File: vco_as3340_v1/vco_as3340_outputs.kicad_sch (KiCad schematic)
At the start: 28 parts, among them J102 SAWTOOTH, J103 TRIANGLE, J104 PULSE, U4 TL072, U5 TL072

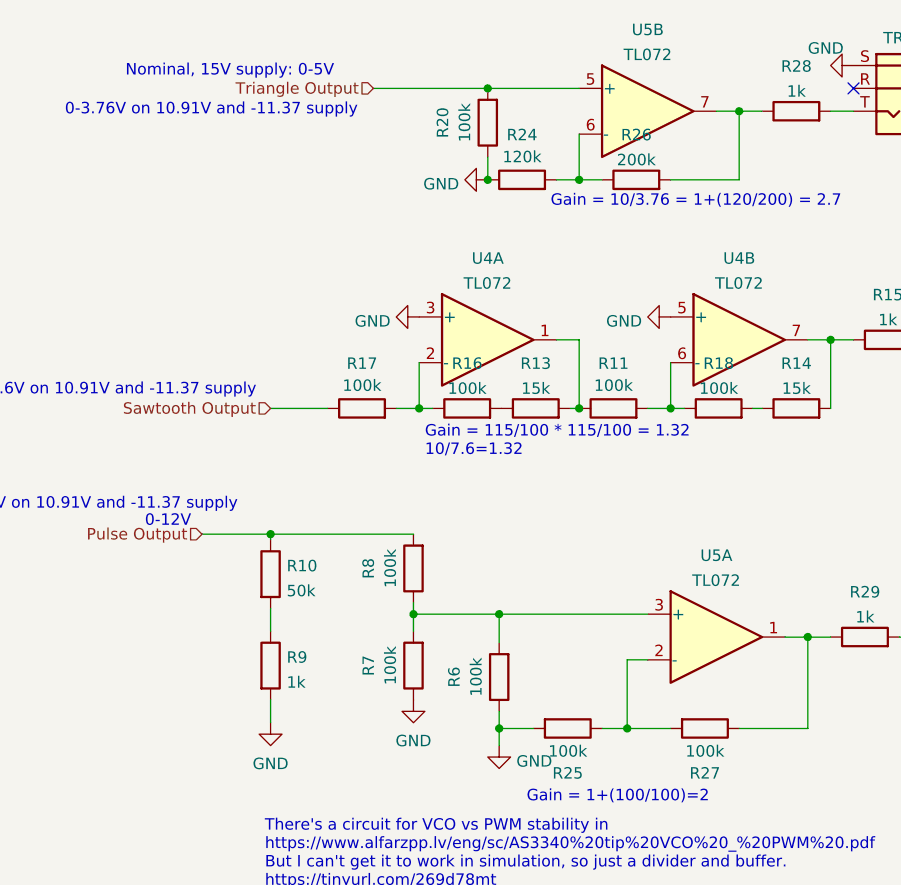
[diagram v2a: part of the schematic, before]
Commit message: Schematic Changes v1 to v2
 - R10 = 47k
 - R9 = 0ohm
 - New C1 100pF across R10 and R9
 - New C15 10uF polarized cap from -5 to GND.
 - R6 DNU
 - R21 & R23 changed to 5.1k
 - RZ1 changed to 18k
 - R26 changed to 100k and new R31 is 100k.
 - New  R32 for 'hysteresis' between PWM and Pulse.
 - Separated grounds on Linear FM and Scale Adj. Circuits for clarity.
 - Added another TL072 (U6) and supporting circuits.
    - This is intended to supply two reference voltages from the 5V
source.
    - The idea is to provide Soft Sync (pin 9) with a stable voltage
of 1/3*Supply, which is something like 11.3/3.
    - The other REF_PITCH2 is for the Linear FM circuit. Some resistors
probably aren't right for this yet, and I think it can completely
replace REF_PITCH pot so I've placed a jumper there to allow either if
it doesn't work out.
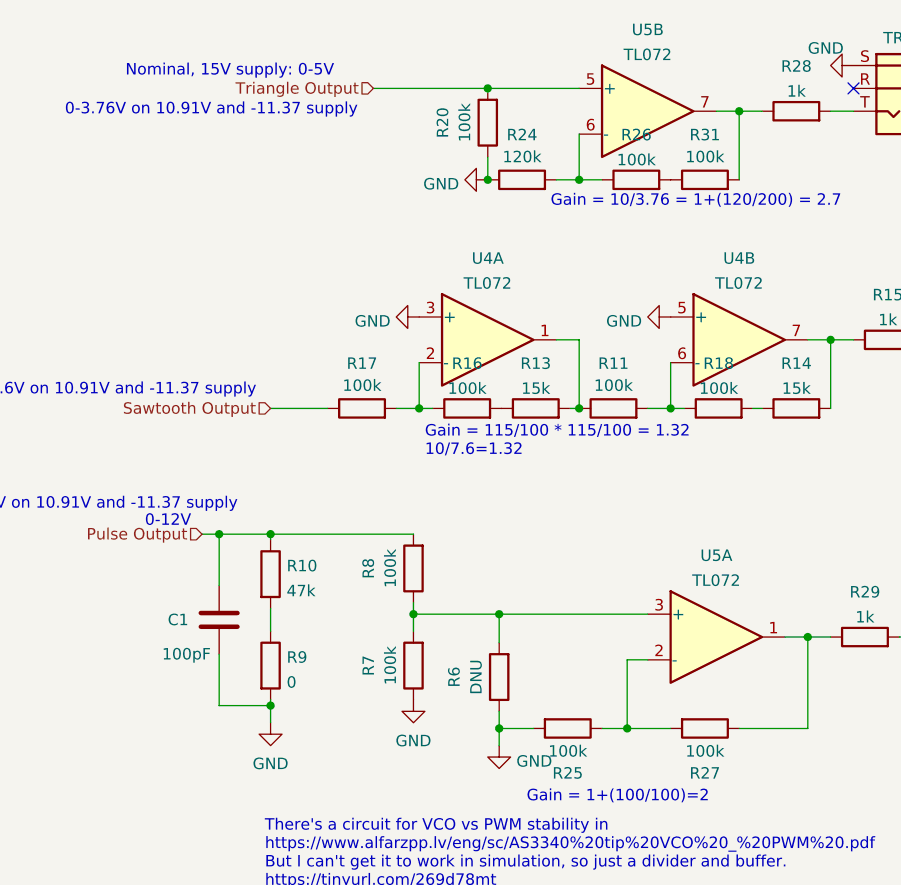
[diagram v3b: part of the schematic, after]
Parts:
- added C1: 100pF, Capacitor_SMD:C_1206_3216Metric_Pad1.33x1.80mm_HandSolder, symbol Device:C
- added R31: 100k, Resistor_SMD:R_1206_3216Metric_Pad1.30x1.75mm_HandSolder, symbol Device:R
- R10: value 50k -> 47k
- R26: value 200k -> 100k
- R6: value 100k -> DNU
- R9: value 1k -> 0
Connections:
- net GND: now also C1.2
- net Pulse Output: now also C1.1
- net at R28.1, U5.7: now also R31.2; no longer R26.2
- new net: R26.2, R31.1
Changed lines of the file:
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@@
     (company "RobotDialogs")
   )
+  (junction (at 77.47 91.44) (diameter 0) (color 0 0 0 0)
+  )
   (junction (at 129.54 25.4) (diameter 0) (color 0 0 0 0)
   )
@@
   )
   (junction (at 111.76 33.02) (diameter 0) (color 0 0 0 0)
+  )
+  (junction (at 71.755 72.39) (diameter 0) (color 0 0 0 0)
   )
   (junction (at 133.985 158.75) (diameter 0) (color 0 0 0 0)
@@
     (stroke (width 0) (type default) (color 0 0 0 0))
   )
+  (wire (pts (xy 71.755 91.44) (xy 77.47 91.44))
+    (stroke (width 0) (type default) (color 0 0 0 0))
+  )
   (wire (pts (xy 109.22 33.02) (xy 111.76 33.02))
     (stroke (width 0) (type default) (color 0 0 0 0))
@@
     (stroke (width 0) (type default) (color 0 0 0 0))
   )
+  (wire (pts (xy 71.755 85.725) (xy 71.755 91.44))
+    (stroke (width 0) (type default) (color 0 0 0 0))
+  )
   (wire (pts (xy 119.38 58.42) (xy 121.92 58.42))
     (stroke (width 0) (type default) (color 0 0 0 0))
@@
     (stroke (width 0) (type default) (color 0 0 0 0))
   )
-  (wire (pts (xy 69.85 72.39) (xy 77.47 72.39))
+  (wire (pts (xy 69.85 72.39) (xy 71.755 72.39))
     (stroke (width 0) (type default) (color 0 0 0 0))
   )
@@
     (stroke (width 0) (type default) (color 0 0 0 0))
   )
-  (wire (pts (xy 121.92 33.02) (xy 129.54 33.02))
-    (stroke (width 0) (type default) (color 0 0 0 0))
-  )
   (wire (pts (xy 93.98 53.34) (xy 93.98 58.42))
     (stroke (width 0) (type default) (color 0 0 0 0))
@@
     (stroke (width 0) (type default) (color 0 0 0 0))
   )
+  (wire (pts (xy 77.47 91.44) (xy 77.47 90.805))
+    (stroke (width 0) (type default) (color 0 0 0 0))
+  )
   (wire (pts (xy 153.67 83.82) (xy 147.32 83.82))
     (stroke (width 0) (type default) (color 0 0 0 0))
@@
     (stroke (width 0) (type default) (color 0 0 0 0))
   )
+  (wire (pts (xy 71.755 78.105) (xy 71.755 72.39))
+    (stroke (width 0) (type default) (color 0 0 0 0))
+  )
   (wire (pts (xy 91.44 58.42) (xy 93.98 58.42))
     (stroke (width 0) (type default) (color 0 0 0 0))
@@
     (stroke (width 0) (type default) (color 0 0 0 0))
   )
+  (wire (pts (xy 71.755 72.39) (xy 77.47 72.39))
+    (stroke (width 0) (type default) (color 0 0 0 0))
+  )
   (wire (pts (xy 102.87 84.455) (xy 102.87 81.28))
     (stroke (width 0) (type default) (color 0 0 0 0))
@@
     (stroke (width 0) (type default) (color 0 0 0 0))
   )
-  (wire (pts (xy 77.47 93.345) (xy 77.47 90.805))
+  (wire (pts (xy 77.47 93.345) (xy 77.47 91.44))
     (stroke (width 0) (type default) (color 0 0 0 0))
   )
@@
     (in_bom yes) (on_board yes) (fields_autoplaced)
     (property "Reference" "R26" (id 0) (at 118.11 28.0375 90))
-    (property "Value" "200k" (id 1) (at 118.11 30.8126 90))
+    (property "Value" "100k" (id 1) (at 118.11 30.8126 90))
     (property "Footprint" "Resistor_SMD:R_1206_3216Metric_Pad1.30x1.75mm_HandSolder" (id 2) (at 118.11 34.798 90)
       (effects (font (size 1.27 1.27)) hide)
@@
     (pin "2")
   )
+  (symbol (lib_id "Device:C") (at 71.755 81.915 0) (unit 1)
+    (in_bom yes) (on_board yes)
+    (property "Reference" "C1" (id 0) (at 66.04 81.915 0)
+      (effects (font (size 1.27 1.27)) (justify left))
+    )
+    (property "Value" "100pF" (id 1) (at 65.405 85.725 0)
+      (effects (font (size 1.27 1.27)) (justify left))
+    )
+    (property "Footprint" "Capacitor_SMD:C_1206_3216Metric_Pad1.33x1.80mm_HandSolder" (id 2) (at 72.7202 85.725 0)
+      (effects (font (size 1.27 1.27)) hide)
+    )
+    (property "Datasheet" "~" (id 3) (at 71.755 81.915 0)
+      (effects (font (size 1.27 1.27)) hide)
+    )
+    (pin "1")
+    (pin "2")
+  )
   (symbol (lib_id "Device:R") (at 77.47 86.995 0) (unit 1)
     (in_bom yes) (on_board yes) (fields_autoplaced)
@@
       (effects (font (size 1.27 1.27)) (justify left))
     )
-    (property "Value" "1k" (id 1) (at 79.248 88.8616 0)
+    (property "Value" "0" (id 1) (at 79.248 88.8616 0)
       (effects (font (size 1.27 1.27)) (justify left))
     )
@@
     (in_bom yes) (on_board yes)
     (property "Reference" "R6" (id 0) (at 97.8875 88.265 90))
-    (property "Value" "100k" (id 1) (at 100.33 88.265 90))
+    (property "Value" "DNU" (id 1) (at 100.33 88.265 90))
     (property "Footprint" "Resistor_SMD:R_1206_3216Metric_Pad1.30x1.75mm_HandSolder" (id 2) (at 104.648 88.265 90)
       (effects (font (size 1.27 1.27)) hide)
@@
     (pin "1")
   )
+  (symbol (lib_id "Device:R") (at 125.73 33.02 90) (unit 1)
+    (in_bom yes) (on_board yes)
+    (property "Reference" "R31" (id 0) (at 125.73 28.0375 90))
+    (property "Value" "100k" (id 1) (at 125.73 30.48 90))
+    (property "Footprint" "Resistor_SMD:R_1206_3216Metric_Pad1.30x1.75mm_HandSolder" (id 2) (at 125.73 34.798 90)
+      (effects (font (size 1.27 1.27)) hide)
+    )
+    (property "Datasheet" "~" (id 3) (at 125.73 33.02 0)
+      (effects (font (size 1.27 1.27)) hide)
+    )
+    (pin "1")
+    (pin "2")
+  )
   (symbol (lib_id "Device:C") (at 133.985 154.94 0) (unit 1)
     (in_bom yes) (on_board yes) (fields_autoplaced)
@@
       (effects (font (size 1.27 1.27)) (justify left))
     )
-    (property "Value" "50k" (id 1) (at 79.248 78.7016 0)
-      (effects (font (size 1.27 1.27)) (justify left))
-    )
+    (property "Value" "47k" (id 1) (at 79.248 78.7016 0)
+      (effects (font (size 1.27 1.27)) (justify left))
+    )

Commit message: v2 re-layout pcb
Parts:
- removed C13, C17: 10nF, Capacitor_SMD:C_1206_3216Metric_Pad1.33x1.80mm_HandSolder, symbol Device:C
- removed U4, U5: TL072, Package_DIP:DIP-8_W7.62mm_Socket_LongPads, symbol Amplifier_Operational:TL072
- added U4: TL074, Package_DIP:DIP-14_W7.62mm_Socket_LongPads, symbol Amplifier_Operational:TL074
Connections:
- net +12V: now also U4.4 (V+)
- net -12V: now also U4.11 (V-)
- net GND: now also U4.10 (+), U4.12 (+)
- net Triangle Output: now also U4.3 (+)
- net at R27.1, R29.1: now also U4.7
- net at R25.1, R27.2: now also U4.6 (-)
- net at R11.1, R13.2: now also U4.8
- net at R14.2, R15.1: now also U4.14
- net at R28.1, R31.2: now also U4.1
- net at R16.1, R17.2: now also U4.9 (-)
- net at R6.2, R7.2, R8.1: now also U4.5 (+)
- net at R24.2, R26.1: now also U4.2 (-)
- net at R11.2, R18.1: now also U4.13 (-)

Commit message: Changes to v2 from testing
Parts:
- added C13, C17, C19: 10pF, Capacitor_SMD:C_1206_3216Metric_Pad1.33x1.80mm_HandSolder, symbol Device:C
- R8: value 100k -> 110k
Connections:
- net at R27.1, R29.1, U4.7: now also C19.2
- net at R25.1, R27.2, U4.6 (-): now also C19.1
- net at R11.1, R13.2, U4.8: now also C13.2
- net at R14.2, R15.1, U4.14: now also C17.2
- net at R16.1, R17.2, U4.9 (-): now also C13.1
- net at R11.2, R18.1, U4.13 (-): now also C17.1
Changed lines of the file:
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@@
   (title_block
     (title "3340_VCO")
-    (date "2022-12-09")
-    (rev "2.0")
+    (date "2023-01-09")
+    (rev "2.1")
     (company "RobotDialogs")
   )
@@
   (junction (at 77.47 72.39) (diameter 0) (color 0 0 0 0)
   )
+  (junction (at 139.7 58.42) (diameter 0) (color 0 0 0 0)
+  )
   (junction (at 107.95 151.13) (diameter 0) (color 0 0 0 0)
+  )
+  (junction (at 137.16 93.98) (diameter 0) (color 0 0 0 0)
   )
   (junction (at 111.76 58.42) (diameter 0) (color 0 0 0 0)
@@
     (stroke (width 0) (type default) (color 0 0 0 0))
   )
+  (wire (pts (xy 139.7 66.04) (xy 139.7 58.42))
+    (stroke (width 0) (type default) (color 0 0 0 0))
+  )
   (wire (pts (xy 127 25.4) (xy 129.54 25.4))
     (stroke (width 0) (type default) (color 0 0 0 0))
@@
     (stroke (width 0) (type default) (color 0 0 0 0))
   )
+  (wire (pts (xy 121.92 58.42) (xy 121.92 66.04))
+    (stroke (width 0) (type default) (color 0 0 0 0))
+  )
   (wire (pts (xy 109.22 33.02) (xy 111.76 33.02))
     (stroke (width 0) (type default) (color 0 0 0 0))
   )
+  (wire (pts (xy 111.76 66.04) (xy 111.76 58.42))
+    (stroke (width 0) (type default) (color 0 0 0 0))
+  )
   (wire (pts (xy 77.47 80.645) (xy 77.47 83.185))
     (stroke (width 0) (type default) (color 0 0 0 0))
@@
     (stroke (width 0) (type default) (color 0 0 0 0))
   )
+  (wire (pts (xy 93.98 66.04) (xy 99.06 66.04))
+    (stroke (width 0) (type default) (color 0 0 0 0))
+  )
   (wire (pts (xy 137.16 93.98) (xy 129.54 93.98))
     (stroke (width 0) (type default) (color 0 0 0 0))
@@
     (stroke (width 0) (type default) (color 0 0 0 0))
   )
+  (wire (pts (xy 117.094 104.14) (xy 117.094 93.98))
+    (stroke (width 0) (type default) (color 0 0 0 0))
+  )
   (wire (pts (xy 131.064 58.42) (xy 132.08 58.42))
     (stroke (width 0) (type default) (color 0 0 0 0))
@@
     (stroke (width 0) (type default) (color 0 0 0 0))
   )
+  (wire (pts (xy 93.98 58.42) (xy 93.98 66.04))
+    (stroke (width 0) (type default) (color 0 0 0 0))
+  )
   (wire (pts (xy 93.345 81.28) (xy 93.345 83.185))
     (stroke (width 0) (type default) (color 0 0 0 0))
@@
     (stroke (width 0) (type default) (color 0 0 0 0))
   )
+  (wire (pts (xy 106.68 66.04) (xy 111.76 66.04))
+    (stroke (width 0) (type default) (color 0 0 0 0))
+  )
   (wire (pts (xy 111.76 58.42) (xy 111.76 50.8))
     (stroke (width 0) (type default) (color 0 0 0 0))
@@
     (stroke (width 0) (type default) (color 0 0 0 0))
   )
+  (wire (pts (xy 137.16 93.98) (xy 137.16 104.14))
+    (stroke (width 0) (type default) (color 0 0 0 0))
+  )
+  (wire (pts (xy 121.92 66.04) (xy 124.714 66.04))
+    (stroke (width 0) (type default) (color 0 0 0 0))
+  )
   (wire (pts (xy 121.92 93.98) (xy 117.094 93.98))
     (stroke (width 0) (type default) (color 0 0 0 0))
@@
     (stroke (width 0) (type default) (color 0 0 0 0))
   )
+  (wire (pts (xy 132.334 66.04) (xy 139.7 66.04))
+    (stroke (width 0) (type default) (color 0 0 0 0))
+  )
   (wire (pts (xy 101.6 30.48) (xy 101.6 33.02))
     (stroke (width 0) (type default) (color 0 0 0 0))
@@
     (stroke (width 0) (type default) (color 0 0 0 0))
   )
+  (wire (pts (xy 121.92 104.14) (xy 117.094 104.14))
+    (stroke (width 0) (type default) (color 0 0 0 0))
+  )
   (wire (pts (xy 102.87 84.455) (xy 102.87 81.28))
     (stroke (width 0) (type default) (color 0 0 0 0))
@@
     (stroke (width 0) (type default) (color 0 0 0 0))
   )
+  (wire (pts (xy 129.54 104.14) (xy 137.16 104.14))
+    (stroke (width 0) (type default) (color 0 0 0 0))
+  )
   (wire (pts (xy 160.02 50.8) (xy 149.86 50.8))
     (stroke (width 0) (type default) (color 0 0 0 0))
@@
     (effects (font (size 1.27 1.27)) (justify left bottom))
   )
-  (text "Gain = 1+(100/100)=2" (at 105.918 102.362 0)
+  (text "Gain = 1+(100/100)=2" (at 91.948 103.378 0)
     (effects (font (size 1.27 1.27)) (justify left bottom))
   )
@@
   )
   (text "There's a circuit for VCO vs PWM stability in\nhttps://www.alfarzpp.lv/eng/sc/AS3340%20tip%20VCO%20_%20PWM%20.pdf\nBut I can't get it to work in simulation, so just a divider and buffer.\nhttps://tinyurl.com/269d78mt"
-    (at 76.835 111.76 0)
+    (at 74.676 121.158 0)
     (effects (font (size 1.27 1.27)) (justify left bottom))
   )
@@
     (in_bom yes) (on_board yes)
     (property "Reference" "R8" (id 0) (at 88.3625 76.2 90))
-    (property "Value" "100k" (id 1) (at 90.805 76.2 90))
+    (property "Value" "110k" (id 1) (at 90.805 76.2 90))
     (property "Footprint" "Resistor_SMD:R_1206_3216Metric_Pad1.30x1.75mm_HandSolder" (id 2) (at 95.123 76.2 90)
       (effects (font (size 1.27 1.27)) hide)
@@
     (pin "1")
   )
+  (symbol (lib_id "Device:C") (at 125.73 104.14 90) (unit 1)
+    (in_bom yes) (on_board yes)
+    (property "Reference" "C19" (id 0) (at 125.73 109.855 0)
+      (effects (font (size 1.27 1.27)) (justify left))
+    )
+    (property "Value" "10pF" (id 1) (at 129.54 110.49 0)
+      (effects (font (size 1.27 1.27)) (justify left))
+    )
+    (property "Footprint" "Capacitor_SMD:C_1206_3216Metric_Pad1.33x1.80mm_HandSolder" (id 2) (at 129.54 103.1748 0)
+      (effects (font (size 1.27 1.27)) hide)
+    )
+    (property "Datasheet" "~" (id 3) (at 125.73 104.14 0)
+      (effects (font (size 1.27 1.27)) hide)
+    )
+    (pin "1")
+    (pin "2")
+  )
   (symbol (lib_id "power:GND") (at 107.95 151.13 90) (unit 1)
     (in_bom yes) (on_board yes) (fields_autoplaced)
@@
     (pin "7")
   )
+  (symbol (lib_id "Device:C") (at 102.87 66.04 90) (unit 1)
+    (in_bom yes) (on_board yes)
+    (property "Reference" "C13" (id 0) (at 102.87 71.755 0)
+      (effects (font (size 1.27 1.27)) (justify left))
+    )
+    (property "Value" "10pF" (id 1) (at 106.68 72.39 0)
+      (effects (font (size 1.27 1.27)) (justify left))
+    )
+    (property "Footprint" "Capacitor_SMD:C_1206_3216Metric_Pad1.33x1.80mm_HandSolder" (id 2) (at 106.68 65.0748 0)
+      (effects (font (size 1.27 1.27)) hide)
+    )
+    (property "Datasheet" "~" (id 3) (at 102.87 66.04 0)
+      (effects (font (size 1.27 1.27)) hide)
+    )
+    (pin "1")
+    (pin "2")
+  )
   (symbol (lib_id "Device:R") (at 135.89 58.42 90) (unit 1)
     (in_bom yes) (on_board yes) (fields_autoplaced)
@@
       (effects (font (size 1.27 1.27)) hide)
     )
+    (pin "1")
+    (pin "2")
+  )
+  (symbol (lib_id "Device:C") (at 128.524 66.04 90) (unit 1)
+    (in_bom yes) (on_board yes)
+    (property "Reference" "C17" (id 0) (at 128.524 71.755 0)
+      (effects (font (size 1.27 1.27)) (justify left))
+    )
+    (property "Value" "10pF" (id 1) (at 132.334 72.39 0)
+      (effects (font (size 1.27 1.27)) (justify left))
+    )
+    (property "Footprint" "Capacitor_SMD:C_1206_3216Metric_Pad1.33x1.80mm_HandSolder" (id 2) (at 132.334 65.0748 0)
+      (effects (font (size 1.27 1.27)) hide)
+    )
+    (property "Datasheet" "~" (id 3) (at 128.524 66.04 0)
+      (effects (font (size 1.27 1.27)) hide)
+    )
